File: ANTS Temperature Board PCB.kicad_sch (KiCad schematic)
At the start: 20 parts, among them J1 1751251, J2 1751251, J3 EBWA-02-A, J4 EBWA-02-A, J5 EBWA-02-A, J6 B2B-XH-A, J7 B2B-XH-A, Q1 IRLZ34N, Q2 IRLZ34N, U1 RASPBERRY_PI_PICO

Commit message: Changed layout a bit to prevent wiring overlap.
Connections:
- net SIGNAL2: now also U1.29 (GP22); no longer U1.32 (GP27_A1)
- net mosfet1_gate: now also U1.32 (GP27_A1); no longer U1.29 (GP22)
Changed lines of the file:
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@@
+	(wire
+		(pts
+			(xy 186.69 78.74) (xy 186.69 80.01)
+		)
+		(stroke
+			(width 0)
+			(type default)
+		)
+	)
+	(wire
+		(pts
+			(xy 177.8 124.46) (xy 176.53 124.46)
+		)
+		(stroke
+			(width 0)
+			(type default)
+		)
+	)
+	(wire
+		(pts
+			(xy 135.89 69.85) (xy 135.89 71.12)
+		)
+		(stroke
+			(width 0)
+			(type default)
+		)
+	)
 	(wire
 		(pts
@@
 	(wire
 		(pts
-			(xy 186.69 78.74) (xy 186.69 80.01)
-		)
-		(stroke
-			(width 0)
-			(type default)
-		)
-	)
-	(wire
-		(pts
-			(xy 177.8 124.46) (xy 176.53 124.46)
-		)
-		(stroke
-			(width 0)
-			(type default)
-		)
-	)
-	(wire
-		(pts
-			(xy 135.89 69.85) (xy 135.89 71.12)
-		)
-		(stroke
-			(width 0)
-			(type default)
-		)
-	)
-	(wire
-		(pts
 			(xy 154.94 116.84) (xy 167.64 116.84)
 		)
@@
 	(wire
 		(pts
+			(xy 92.71 107.95) (xy 92.71 109.22)
+		)
+		(stroke
+			(width 0)
+			(type default)
+		)
+	)
+	(wire
+		(pts
+			(xy 76.2 96.52) (xy 76.2 97.79)
+		)
+		(stroke
+			(width 0)
+			(type default)
+		)
+	)
+	(wire
+		(pts
+			(xy 186.69 66.04) (xy 200.66 66.04)
+		)
+		(stroke
+			(width 0)
+			(type default)
+		)
+	)
+	(wire
+		(pts
+			(xy 105.41 82.55) (xy 92.71 82.55)
+		)
+		(stroke
+			(width 0)
+			(type default)
+		)
+	)
+	(wire
+		(pts
+			(xy 92.71 95.25) (xy 92.71 96.52)
+		)
+		(stroke
+			(width 0)
+			(type default)
+		)
+	)
+	(wire
+		(pts
+			(xy 130.81 107.95) (xy 149.86 107.95)
+		)
+		(stroke
+			(width 0)
+			(type default)
+		)
+	)
+	(wire
+		(pts
+			(xy 186.69 109.22) (xy 200.66 109.22)
+		)
+		(stroke
+			(width 0)
+			(type default)
+		)
+	)
+	(wire
+		(pts
+			(xy 176.53 116.84) (xy 179.07 116.84)
+		)
+		(stroke
+			(width 0)
+			(type default)
+		)
+	)
+	(wire
+		(pts
+			(xy 186.69 111.76) (xy 186.69 109.22)
+		)
+		(stroke
+			(width 0)
+			(type default)
+		)
+	)
+	(wire
+		(pts
+			(xy 105.41 95.25) (xy 92.71 95.25)
+		)
+		(stroke
+			(width 0)
+			(type default)
+		)
+	)
+	(wire
+		(pts
 			(xy 139.7 92.71) (xy 130.81 92.71)
-		)
-		(stroke
-			(width 0)
-			(type default)
-		)
-	)
-	(wire
-		(pts
-			(xy 92.71 107.95) (xy 92.71 109.22)
-		)
-		(stroke
-			(width 0)
-			(type default)
-		)
-	)
-	(wire
-		(pts
-			(xy 76.2 96.52) (xy 76.2 97.79)
-		)
-		(stroke
-			(width 0)
-			(type default)
-		)
-	)
-	(wire
-		(pts
-			(xy 186.69 66.04) (xy 200.66 66.04)
-		)
-		(stroke
-			(width 0)
-			(type default)
-		)
-	)
-	(wire
-		(pts
-			(xy 105.41 82.55) (xy 92.71 82.55)
-		)
-		(stroke
-			(width 0)
-			(type default)
-		)
-	)
-	(wire
-		(pts
-			(xy 92.71 95.25) (xy 92.71 96.52)
-		)
-		(stroke
-			(width 0)
-			(type default)
-		)
-	)
-	(wire
-		(pts
-			(xy 130.81 107.95) (xy 149.86 107.95)
-		)
-		(stroke
-			(width 0)
-			(type default)
-		)
-	)
-	(wire
-		(pts
-			(xy 186.69 109.22) (xy 200.66 109.22)
-		)
-		(stroke
-			(width 0)
-			(type default)
-		)
-	)
-	(wire
-		(pts
-			(xy 176.53 116.84) (xy 179.07 116.84)
-		)
-		(stroke
-			(width 0)
-			(type default)
-		)
-	)
-	(wire
-		(pts
-			(xy 186.69 111.76) (xy 186.69 109.22)
-		)
-		(stroke
-			(width 0)
-			(type default)
-		)
-	)
-	(wire
-		(pts
-			(xy 105.41 95.25) (xy 92.71 95.25)
 		)
 		(stroke
@@
 		)
 	)
-	(label "SIGNAL2"
-		(at 139.7 85.09 180)
-		(effects
-			(font
-				(size 1.27 1.27)
-			)
-			(justify right bottom)
-		)
-	)
 	(label "UART_RX"
 		(at 137.16 110.49 0)
@@
 		)
 	)
-	(label "mosfet1_gate"
-		(at 139.7 92.71 0)
-		(effects
-			(font
-				(size 1.27 1.27)
-			)
-			(justify left bottom)
-		)
-	)
 	(label "VSYS"
 		(at 135.89 67.31 0)
@@
 		)
 	)
+	(label "mosfet1_gate"
+		(at 139.7 85.09 0)
+		(effects
+			(font
+				(size 1.27 1.27)
+			)
+			(justify left bottom)
+		)
+	)
 	(label "UART_TX"
 		(at 137.16 113.03 0)
@@
 		)
 	)
+	(label "SIGNAL2"
+		(at 139.7 92.71 180)
+		(effects
+			(font
+				(size 1.27 1.27)
+			)
+			(justify right bottom)
+		)
+	)

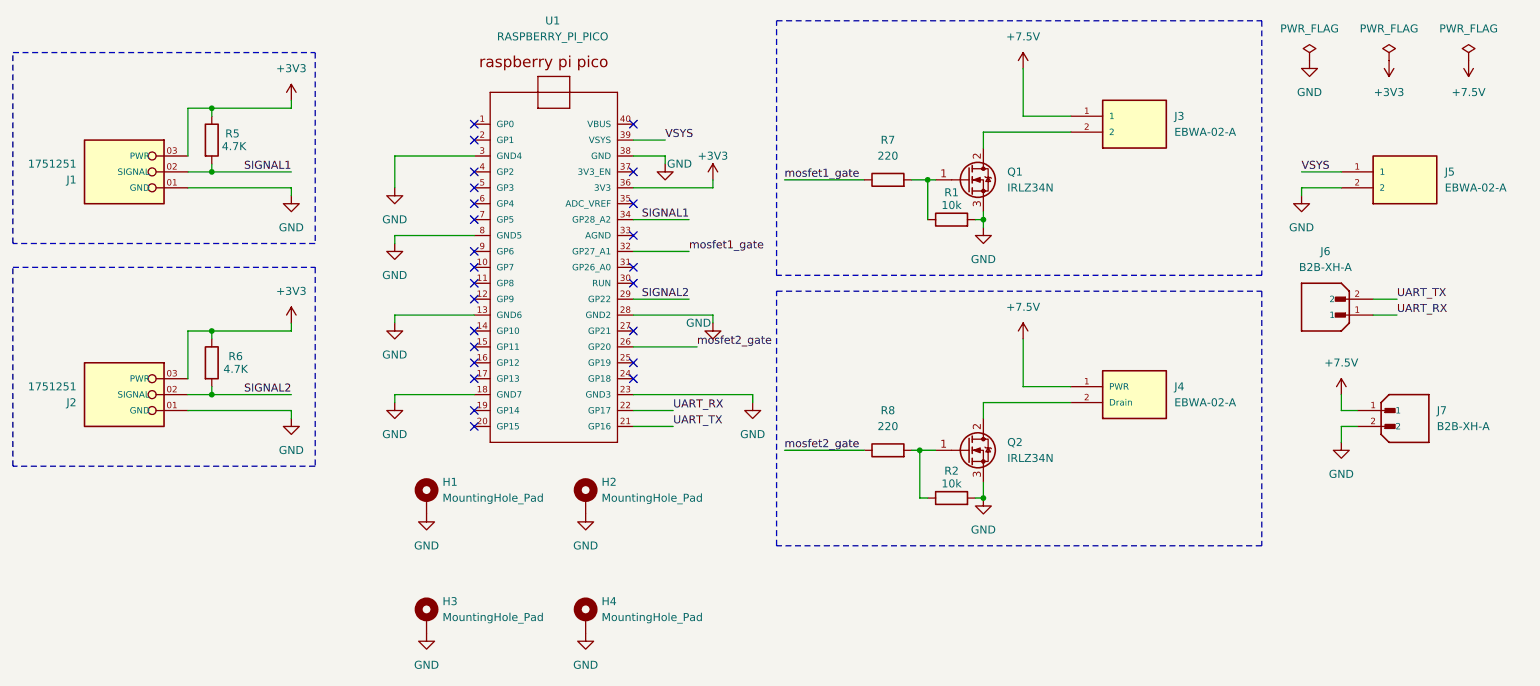
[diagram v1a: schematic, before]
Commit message: deleted one probe and one heater, changed mounting hole footprint to 2.5m holes, and organized board. Also updated schematic.
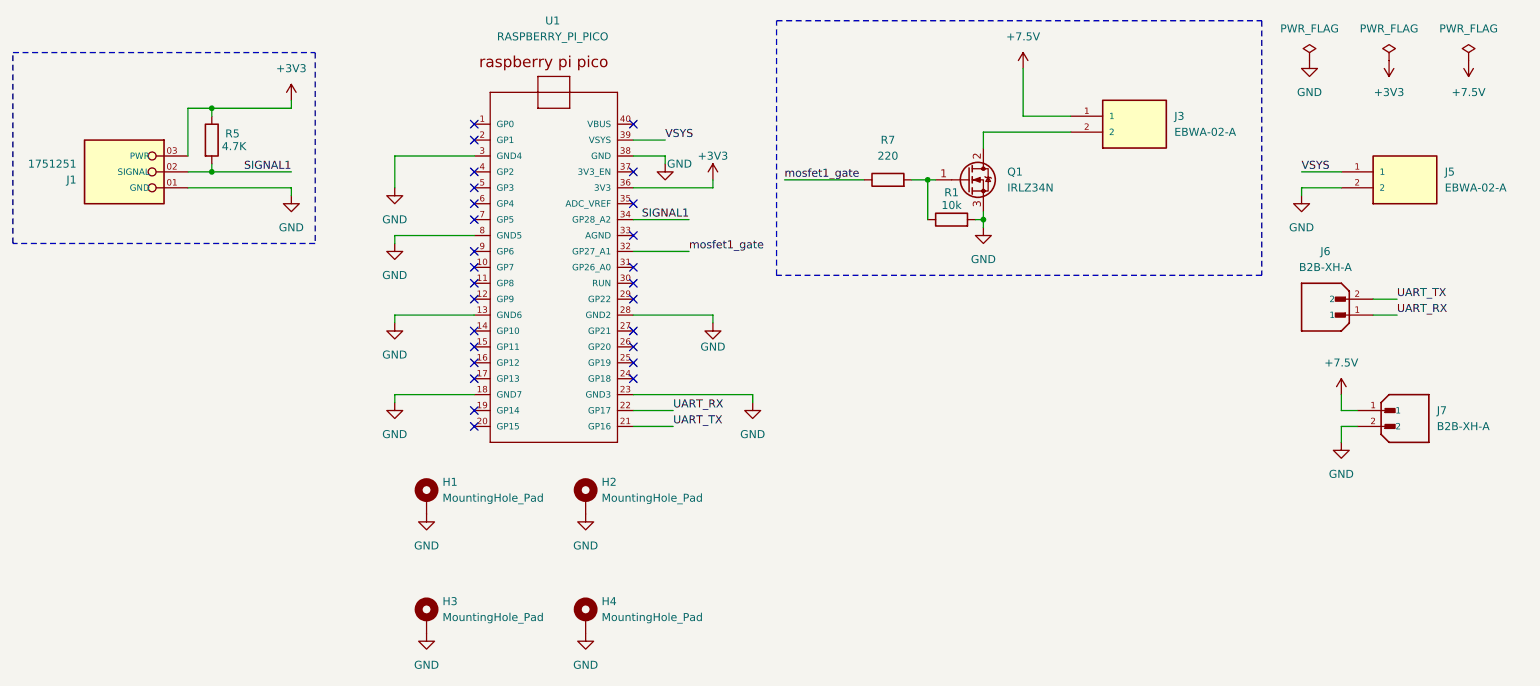
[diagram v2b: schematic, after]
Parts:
- removed J2: 1751251, 67TERM BLOCK:PHOENIX_1751251, symbol TERM BLOCK:1751251
- removed J4: EBWA-02-A, 2 PIN TERM:ADAMTECH_EBWA-02-A, symbol 2 PIN TERM:EBWA-02-A
- removed Q2: IRLZ34N, Package_TO_SOT_THT:TO-220-3_Vertical, symbol Transistor_FET:IRLZ34N
- removed R2: 10k, Resistor_THT:R_Axial_DIN0204_L3.6mm_D1.6mm_P7.62mm_Horizontal, symbol Device:R
- removed R6: 4.7K, Resistor_THT:R_Axial_DIN0204_L3.6mm_D1.6mm_P7.62mm_Horizontal, symbol Device:R
- removed R8: 220, Resistor_THT:R_Axial_DIN0204_L3.6mm_D1.6mm_P7.62mm_Horizontal, symbol Device:R
- H1, H2, H3, H4: footprint MountingHole:MountingHole_2.5mm_Pad_Via -> MountingHole:MountingHole_2.7mm_M2.5_Pad_Via
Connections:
- net SIGNAL2: no longer names the net of U1.29 (GP22)
- net mosfet2_gate: no longer names the net of U1.26 (GP20)
- no-connect marks 25 -> 27

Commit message: Updated mounting holes to M3.
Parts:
- H1, H2, H3, H4: footprint MountingHole:MountingHole_2.7mm_M2.5_Pad_Via -> MountingHole:MountingHole_3.2mm_M3_Pad_Via
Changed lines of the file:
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@@
 			)
 		)
-		(property "Footprint" "MountingHole:MountingHole_2.7mm_M2.5_Pad_Via"
+		(property "Footprint" "MountingHole:MountingHole_3.2mm_M3_Pad_Via"
 			(at 123.19 124.46 0)
 			(hide yes)
@@
 			)
 		)
-		(property "Footprint" "MountingHole:MountingHole_2.7mm_M2.5_Pad_Via"
+		(property "Footprint" "MountingHole:MountingHole_3.2mm_M3_Pad_Via"
 			(at 97.79 143.51 0)
 			(hide yes)
@@
 			)
 		)
-		(property "Footprint" "MountingHole:MountingHole_2.7mm_M2.5_Pad_Via"
+		(property "Footprint" "MountingHole:MountingHole_3.2mm_M3_Pad_Via"
 			(at 123.19 143.51 0)
 			(hide yes)
@@
 			)
 		)
-		(property "Footprint" "MountingHole:MountingHole_2.7mm_M2.5_Pad_Via"
+		(property "Footprint" "MountingHole:MountingHole_3.2mm_M3_Pad_Via"
 			(at 97.79 124.46 0)
 			(hide yes)

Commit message: Fixed small error with difference in footprints.
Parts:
- H1, H2, H3, H4: footprint MountingHole:MountingHole_3.2mm_M3_Pad_Via -> MountingHole:MountingHole_2.7mm_M2.5_Pad_Via
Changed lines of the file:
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@@
 			)
 		)
-		(property "Footprint" "MountingHole:MountingHole_3.2mm_M3_Pad_Via"
+		(property "Footprint" "MountingHole:MountingHole_2.7mm_M2.5_Pad_Via"
 			(at 123.19 124.46 0)
 			(hide yes)
@@
 			)
 		)
-		(property "Footprint" "MountingHole:MountingHole_3.2mm_M3_Pad_Via"
+		(property "Footprint" "MountingHole:MountingHole_2.7mm_M2.5_Pad_Via"
 			(at 97.79 143.51 0)
 			(hide yes)
@@
 			)
 		)
-		(property "Footprint" "MountingHole:MountingHole_3.2mm_M3_Pad_Via"
+		(property "Footprint" "MountingHole:MountingHole_2.7mm_M2.5_Pad_Via"
 			(at 123.19 143.51 0)
 			(hide yes)
@@
 			)
 		)
-		(property "Footprint" "MountingHole:MountingHole_3.2mm_M3_Pad_Via"
+		(property "Footprint" "MountingHole:MountingHole_2.7mm_M2.5_Pad_Via"
 			(at 97.79 124.46 0)
 			(hide yes)
